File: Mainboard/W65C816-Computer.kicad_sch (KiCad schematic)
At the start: 110 parts, among them J1 ADDR_DATA_DBG, J2 CTRL_BANK_DBG, J3 CPU_MISC_DBG, J4 POWER_IN_HEADER_8A, J5 DAUGHTER_PWR_AUX, J6 ISA16_DAUGHTER_BUS, J7 PWR_LED_HEADER, J8 RESET_HEADER, Q1 P-MOSFET_REV_PROT_TO220, SW2 NMI, SW3 MAIN_PWR_SW_EXT, U1 W65C816S6PG-14, U10 SN74HC04N, U11 SN74HC08N, U12 SN74HC139N, U16 SN74HC245N, U17 SN74HC32N, U18 SN74HC04N, U2 SN74HC573N, U20 AS6C4008-55PCN, U21 AS6C4008-55PCN, U22 AS6C4008-55PCN, U23 AS6C4008-55PCN, U24 AS6C4008-55PCN, U25 AS6C4008-55PCN, U26 AS6C4008-55PCN, U27 AS6C4008-55PCN, U3 SN74HC245N, U30 SST39VF040-70-4I-NHE, U4 MCP130-315D, U5 SN74HC14N, U6 SN74HC138N, U7 SN74HC138N, U8 SN74HC138N, U9 SN74HC00N, X1 ECS-P143X-8.000-BN

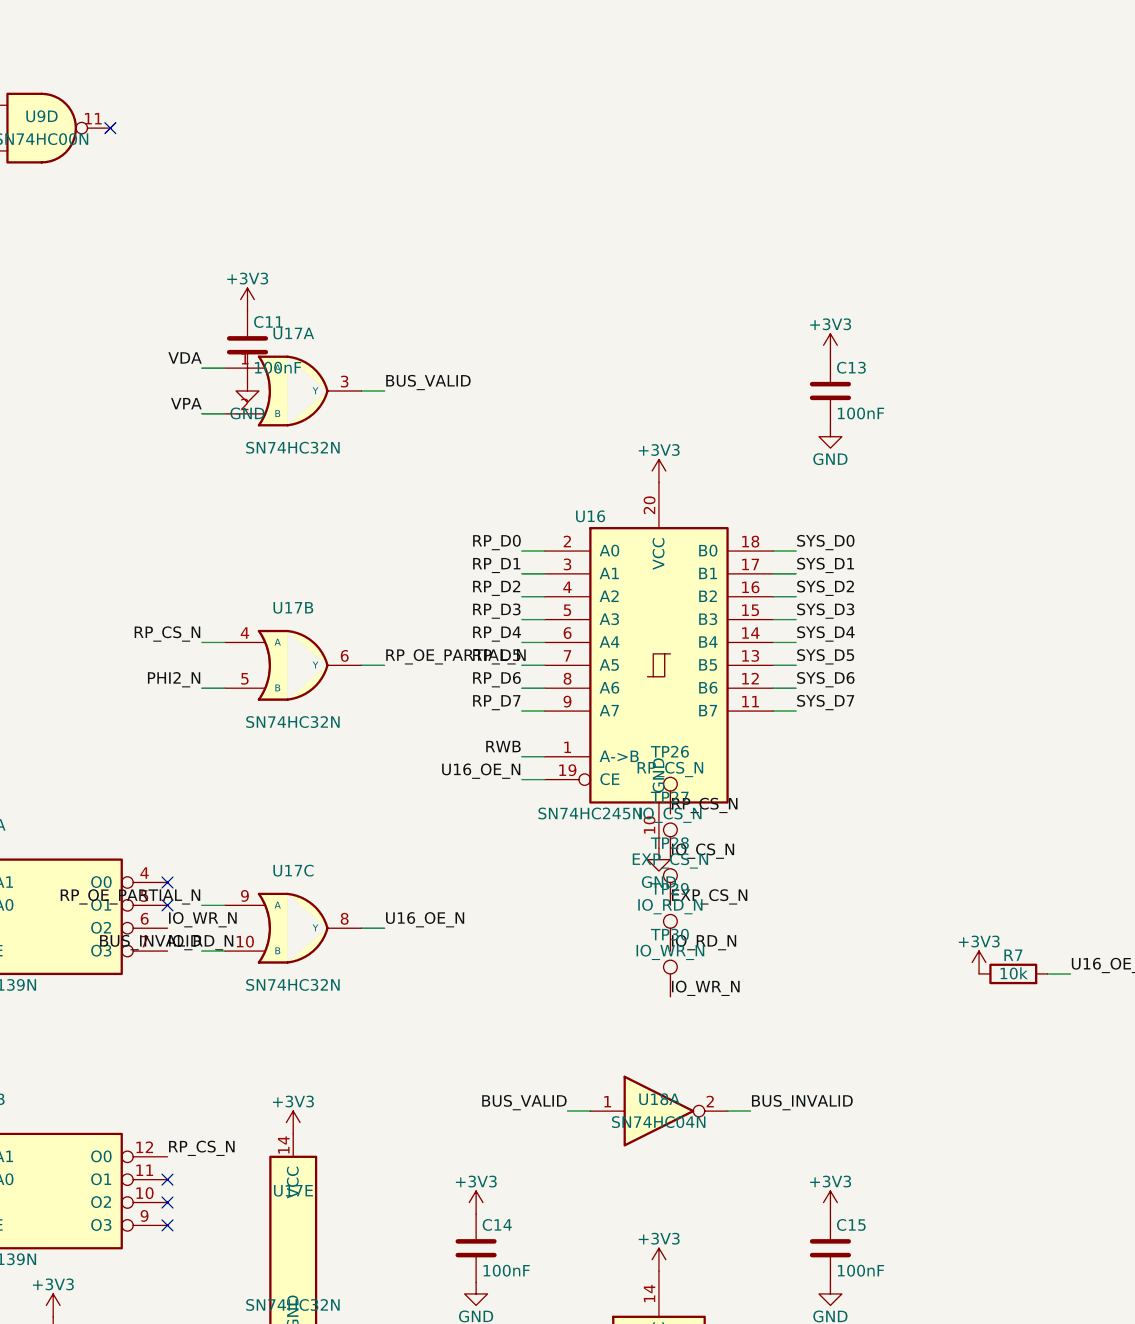
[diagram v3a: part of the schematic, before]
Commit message: Added HDMI and PSRAM
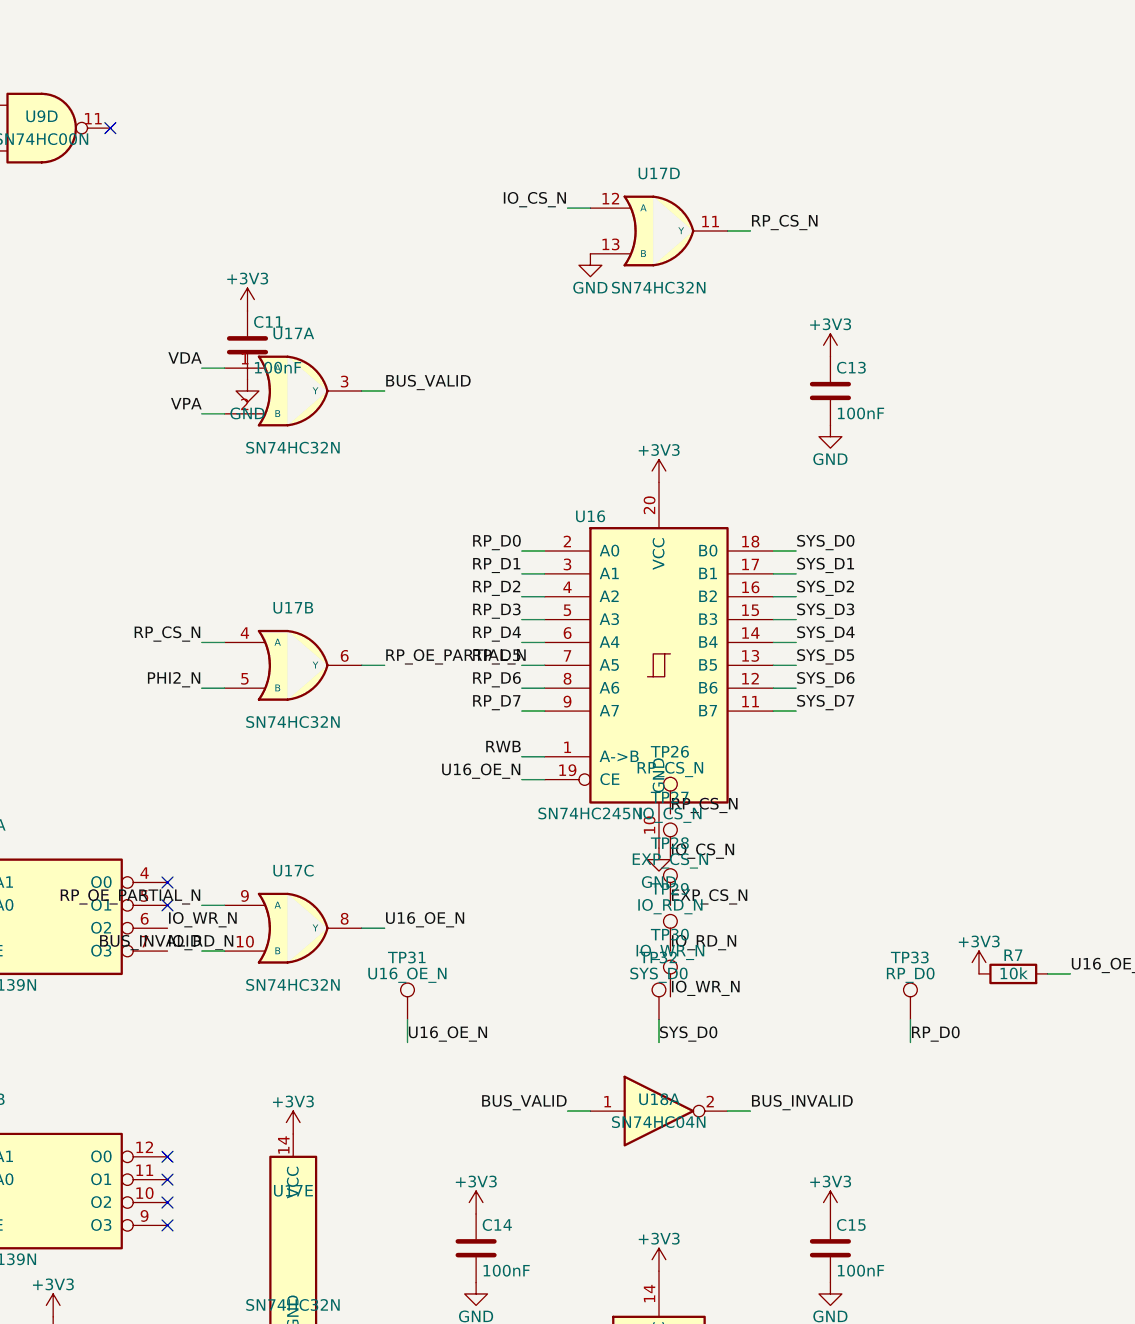
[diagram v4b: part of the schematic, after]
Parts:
- added TP31: U16_OE_N, TestPoint:TestPoint_THTPad_D1.5mm_Drill0.7mm, symbol Connector:TestPoint
- added TP32: SYS_D0, TestPoint:TestPoint_THTPad_D1.5mm_Drill0.7mm, symbol Connector:TestPoint
- added TP33: RP_D0, TestPoint:TestPoint_THTPad_D1.5mm_Drill0.7mm, symbol Connector:TestPoint
- added unit 4 of U17
- U16: footprint (none) -> Package_DIP:DIP-20_W7.62mm_Socket_LongPads
- U17, U18: footprint (none) -> Package_DIP:DIP-14_W7.62mm_Socket_LongPads
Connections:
- net GND: now also U17.13 (B)
- net IO_CS_N: now also U17.12 (A)
- net RP_CS_N: now also U17.11 (Y); no longer U12.12 (O0)
- net RP_D0: now also TP33.1
- net SYS_D0: now also TP32.1
- net U16_OE_N: now also TP31.1
- no-connect marks 47 -> 48

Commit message: Added  missing footprints to mianboard
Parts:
- C13, C14, C15: footprint (none) -> Capacitor_THT:C_Disc_D3.0mm_W1.6mm_P2.50mm
- R7: footprint (none) -> Resistor_THT:R_Axial_DIN0207_L6.3mm_D2.5mm_P7.62mm_Horizontal
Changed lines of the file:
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@@
 			)
 		)
-		(property "Footprint" ""
+		(property "Footprint" "Capacitor_THT:C_Disc_D3.0mm_W1.6mm_P2.50mm"
 			(at 449.58 219.71 0)
 			(hide yes)
@@
 			)
 		)
-		(property "Footprint" ""
+		(property "Footprint" "Capacitor_THT:C_Disc_D3.0mm_W1.6mm_P2.50mm"
 			(at 410.21 314.96 0)
 			(hide yes)
@@
 			)
 		)
-		(property "Footprint" ""
+		(property "Footprint" "Capacitor_THT:C_Disc_D3.0mm_W1.6mm_P2.50mm"
 			(at 449.58 314.96 0)
 			(hide yes)
@@
 			)
 		)
-		(property "Footprint" ""
+		(property "Footprint" "Resistor_THT:R_Axial_DIN0207_L6.3mm_D2.5mm_P7.62mm_Horizontal"
 			(at 469.9 284.48 0)
 			(hide yes)

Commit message: Qualify U3 `/OE` with PHI2.
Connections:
- net GND: no longer U3.19 (CE)
- net PHI2_N: now also U3.19 (CE)
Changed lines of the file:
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@@
 		)
 	)
+	(wire
+		(pts
+			(xy 121.92 180.34)
+			(xy 119.38 180.34)
+		)
+	)
 	(text "Power input: PJ-102A barrel jack is center-positive and rated 2.5 A. +5V is fused, switched, reverse-polarity protected by Q1, TVS-clamped, then feeds the daughterboard power connector and MOD1 3.3 V buck module."
 		(at 19.812 216.154 0)
@@
 	)
 	(label "GND"
-		(at 121.92 180.34 180)
-		(effects
-			(font
-				(size 1.27 1.27)
-			)
-			(justify right bottom)
-		)
-	)
-	(label "GND"
 		(at 261.62 292.1 180)
 		(effects
@@
 		)
 	)
+	(label "PHI2_N"
+		(at 119.38 180.34 180)
+		(effects
+			(font
+				(size 1.27 1.27)
+			)
+			(justify right bottom)
+		)
+	)

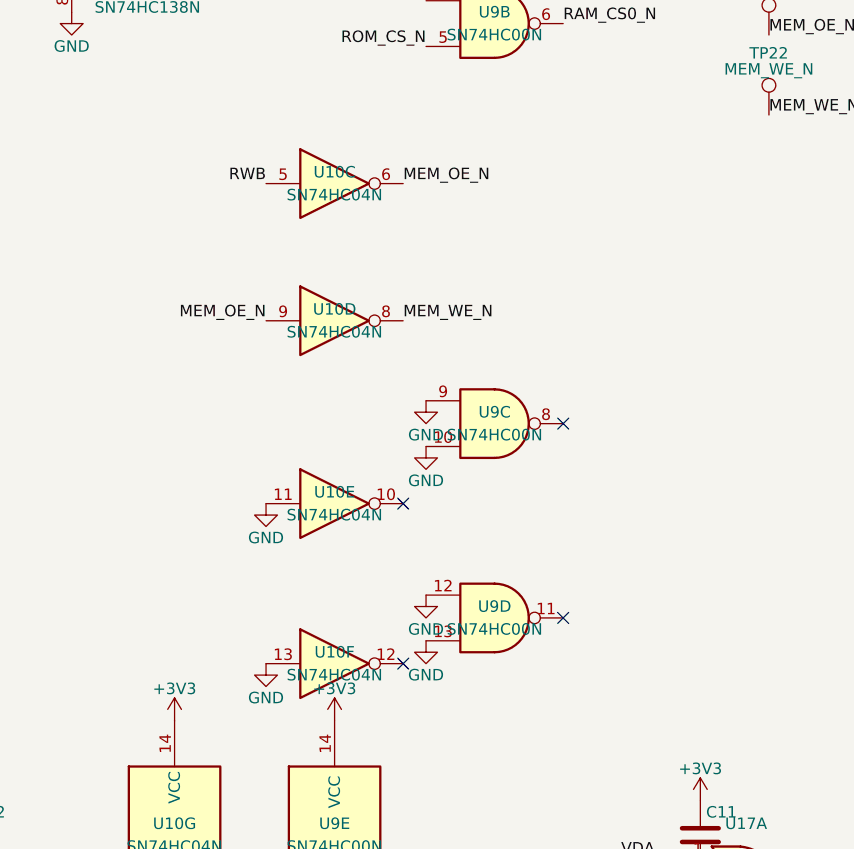
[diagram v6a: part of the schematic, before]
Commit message: Generate PHI2-qualified `MEM_OE_N` and `MEM_WE_N`.
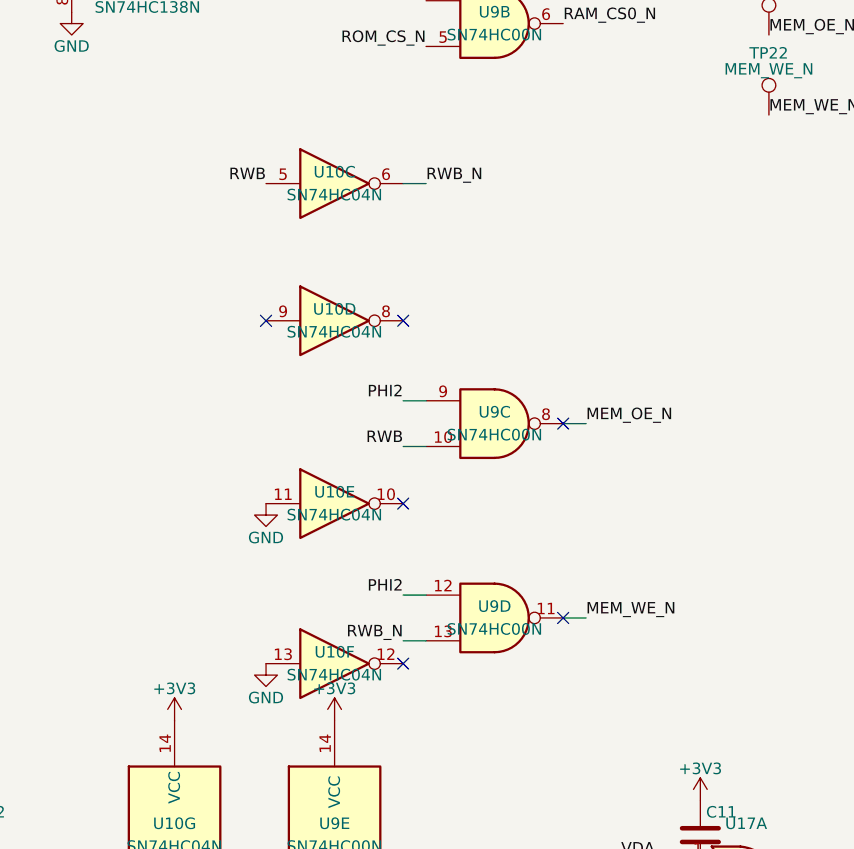
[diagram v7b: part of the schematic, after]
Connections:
- net GND: no longer U9.10, U9.12, U9.13, U9.9
- net MEM_OE_N: now also U9.8; no longer U10.6, U10.9
- net MEM_WE_N: now also U9.11; no longer U10.8
- net PHI2: now also U9.12, U9.9
- net RWB: now also U9.10
- new net RWB_N: U10.6, U9.13
- no-connect marks 48 -> 50

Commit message: Place and terminate unused U18 gates
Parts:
- added unit 3 of U18
- added unit 5 of U18
- added unit 6 of U18
- added unit 4 of U18
- added unit 2 of U18
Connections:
- net GND: now also U18.11, U18.13, U18.3, U18.5, U18.9
- no-connect marks 50 -> 55
